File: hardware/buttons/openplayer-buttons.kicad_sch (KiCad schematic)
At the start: 10 parts, among them J1 CARRIER, SW1 POWER, SW2 VOL+, SW3 VOL-, SW4 PREV, SW5 PLAY, SW6 NEXT, SW7 MENU

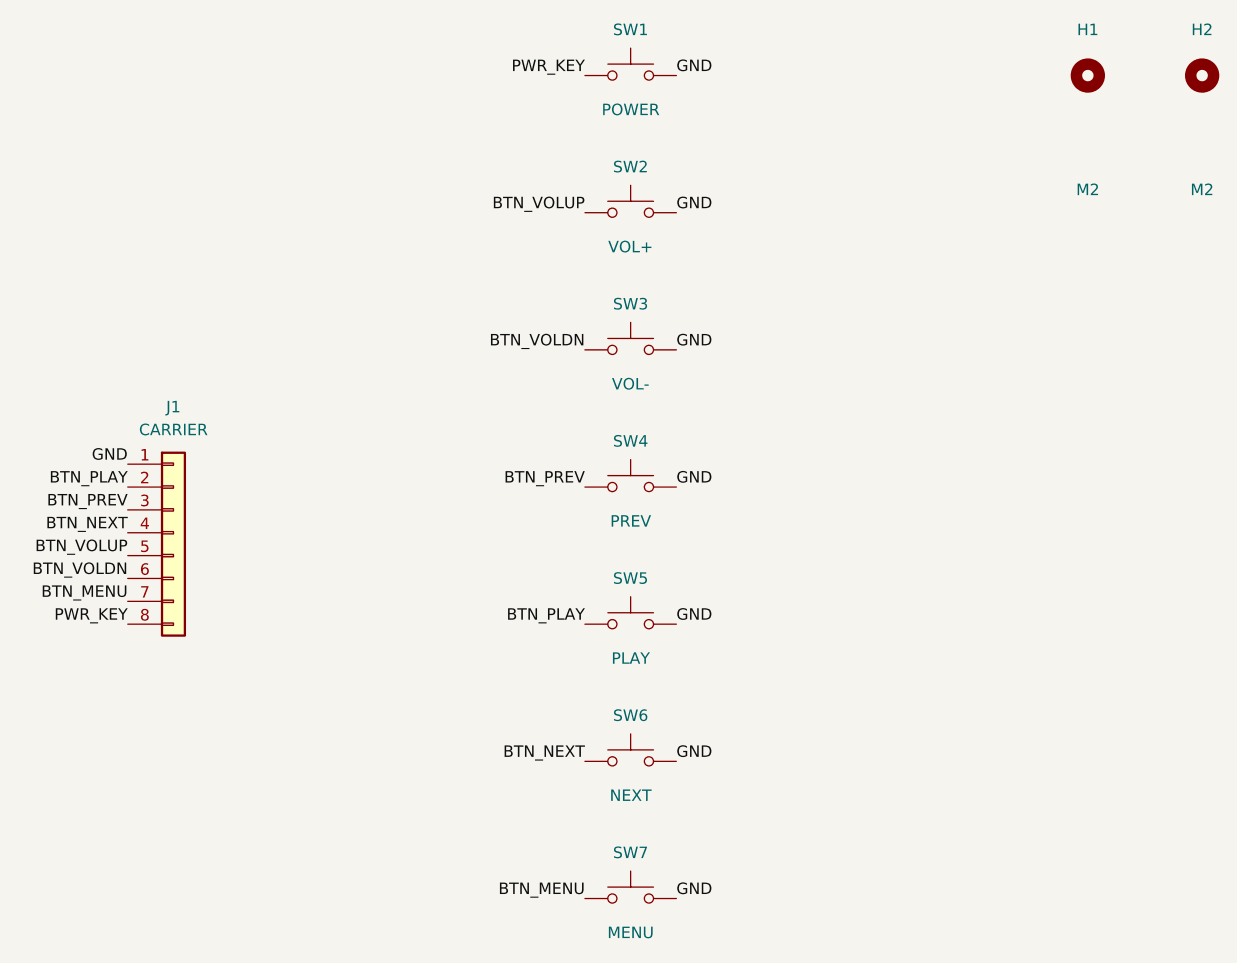
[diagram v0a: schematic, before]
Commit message: Update button and carrier schematics: modify switch positions and add new connector J7
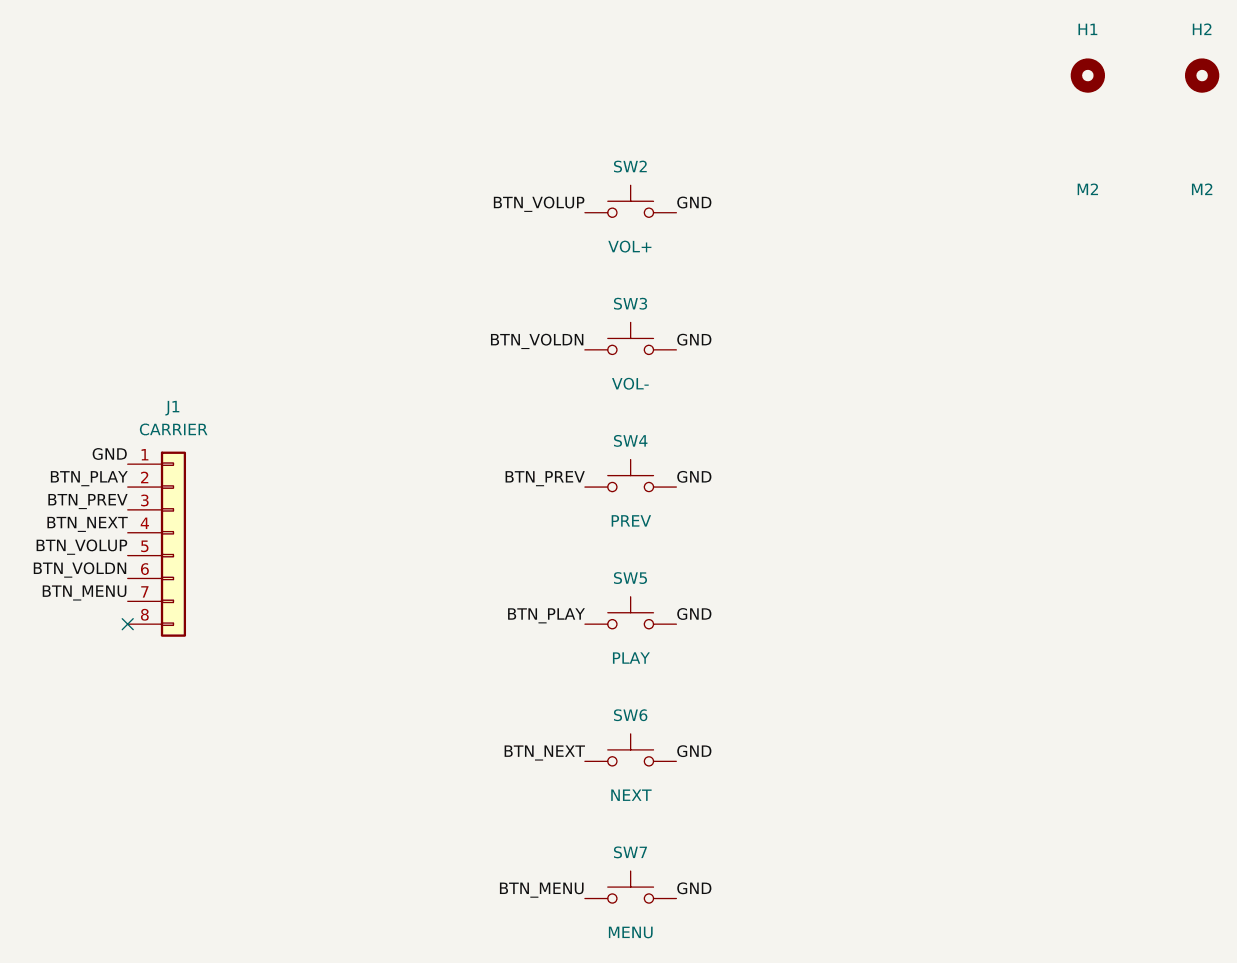
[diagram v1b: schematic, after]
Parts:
- removed SW1: POWER, Button_Switch_THT:SW_PUSH_6mm, symbol Switch:SW_Push
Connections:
- net PWR_KEY: no longer names the net of J1.8 (Pin_8)
- no-connect marks 0 -> 1
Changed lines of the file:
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@@
 (paper "A4")
 (title_block (title "OpenPlayer buttons") (rev "A") (comment 1 "Generated by hardware/buttons/scripts/build_sch.py; do not edit by hand"))
-(symbol (lib_id "Switch:SW_Push") (at 152.40 50.80 0) (unit 1)
-(exclude_from_sim no) (in_bom yes) (on_board yes) (dnp no)
-(property "Reference" "SW1" (at 152.40 45.72 0) (effects (font (size 1.27 1.27))))
-(property "Value" "POWER" (at 152.40 54.61 0) (effects (font (size 1.27 1.27))))
-(property "Footprint" "Button_Switch_THT:SW_PUSH_6mm" (at 152.40 50.80 0) (hide yes) (effects (font (size 1.27 1.27))))
-(property "Datasheet" "" (at 152.40 50.80 0) (hide yes) (effects (font (size 1.27 1.27))))
-(property "Description" "6x6 THT tactile, height per enclosure" (at 152.40 50.80 0) (hide yes) (effects (font (size 1.27 1.27))))
-(pin "1")
-(pin "2")
-(instances (project "openplayer-buttons" (path "/ec122071-abc6-5292-a6b7-15c803da2898" (reference "SW1") (unit 1))))
-)
-(label "PWR_KEY" (at 147.32 50.80 180) (effects (font (size 1.27 1.27)) (justify right bottom)))
-(label "GND" (at 157.48 50.80 0) (effects (font (size 1.27 1.27)) (justify left bottom)))
 (symbol (lib_id "Switch:SW_Push") (at 152.40 66.04 0) (unit 1)
 (exclude_from_sim no) (in_bom yes) (on_board yes) (dnp no)
@@
 (label "BTN_VOLDN" (at 96.52 106.68 180) (effects (font (size 1.27 1.27)) (justify right bottom)))
 (label "BTN_MENU" (at 96.52 109.22 180) (effects (font (size 1.27 1.27)) (justify right bottom)))
-(label "PWR_KEY" (at 96.52 111.76 180) (effects (font (size 1.27 1.27)) (justify right bottom)))
+(no_connect (at 96.52 111.76))
 (symbol (lib_id "Mechanical:MountingHole") (at 203.20 50.80 0) (unit 1)
 (exclude_from_sim no) (in_bom no) (on_board yes) (dnp no)
